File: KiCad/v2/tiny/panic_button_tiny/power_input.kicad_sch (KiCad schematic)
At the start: 3 parts, among them J1 Conn_USB_C_Socket_PowerOnly

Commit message: [UPDATE] the structure of the KiCad design for the tiny version
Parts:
- added U3: ME6211C33M5, Package_TO_SOT_SMD:SOT-23-5, symbol Regulator_Linear:ME6211C33M5
- renumbered J1 to J2
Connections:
- net 5V: now also U3.1 (V_{IN})
- net GND: now also U3.2 (V_{SS})
- new net 3.3V: U3.5 (V_{OUT})
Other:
- added sheet Li-ion charging handling (li-ion_charging_handling.kicad_sch)
- note added: "Voltage stepper for the 3.3v line"

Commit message: [UPDATE] the schematic to contain more connections for the battery section
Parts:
- added C2, C4: 10uF, PCM_SparkFun-Capacitor:C_0603_1608Metric, symbol PCM_SparkFun-Capacitor:10uF_0603_10V_20%
- added C3: 1uF_0603_25V, Capacitor_SMD:C_0201_0603Metric_Pad0.64x0.40mm_HandSolder, symbol PCM_4ms_Capacitor:1uF_0603_25V
- added C5: 100nF_Ceramic, Capacitor_THT:C_Disc_D5.0mm_W2.5mm_P2.50mm, symbol PCM_SL_Capacitors:100nF_Ceramic
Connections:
- net 3.3V: now also C4.1
- net 5V: now also U3.3 (CE), C2.1, C3.2
- net GND: now also C2.2, C3.1, C5.1
- new net: C4.2, C5.2

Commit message: [UPDATE] the schematic wirering
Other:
- sheet Li-ion charging handling ports: added PIN+(5V), PIN-(5V); removed none
- moved on the sheet: C3, C4, C5, U3

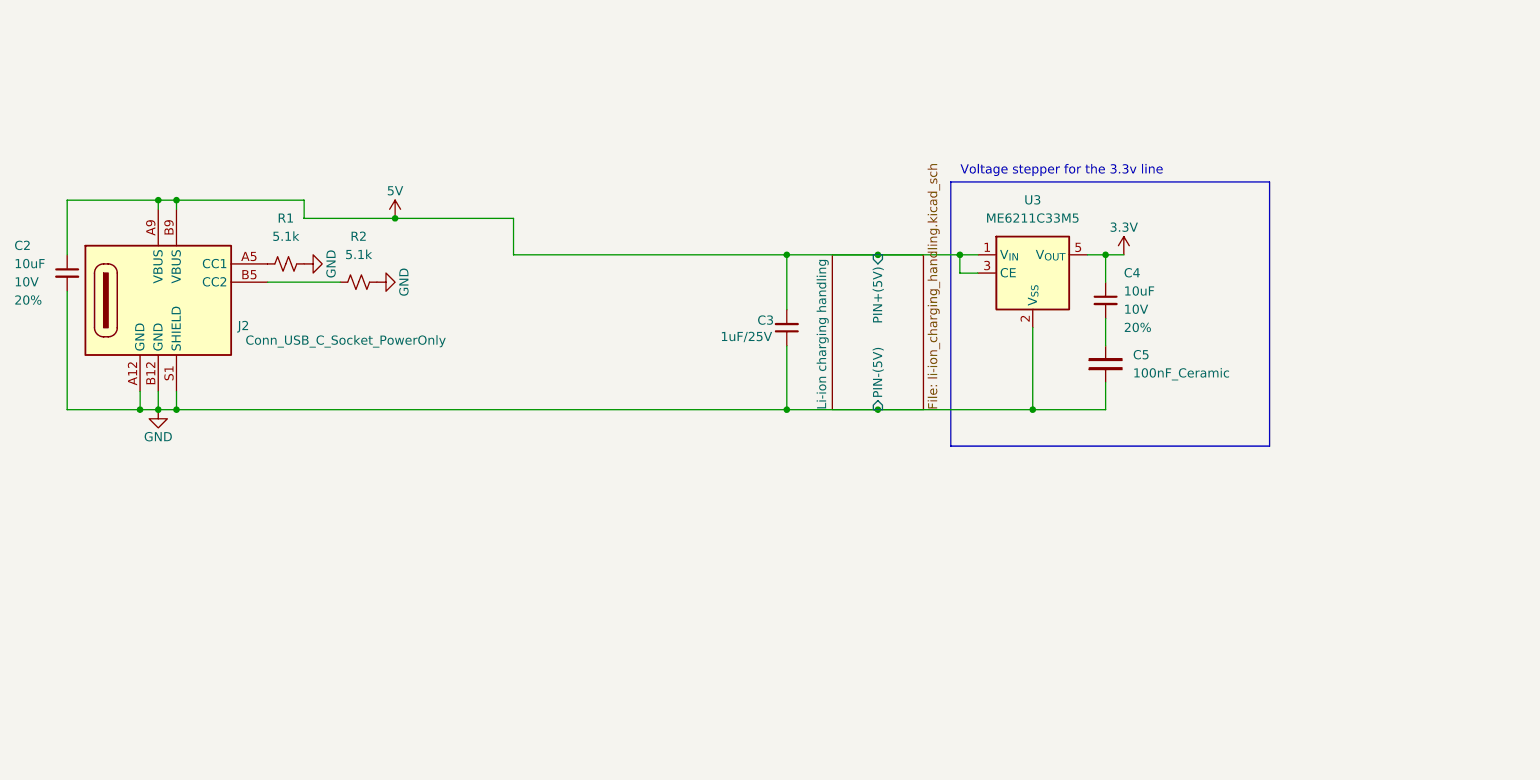
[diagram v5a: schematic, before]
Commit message: [UPDATE] the schematics to hopefully include better connections
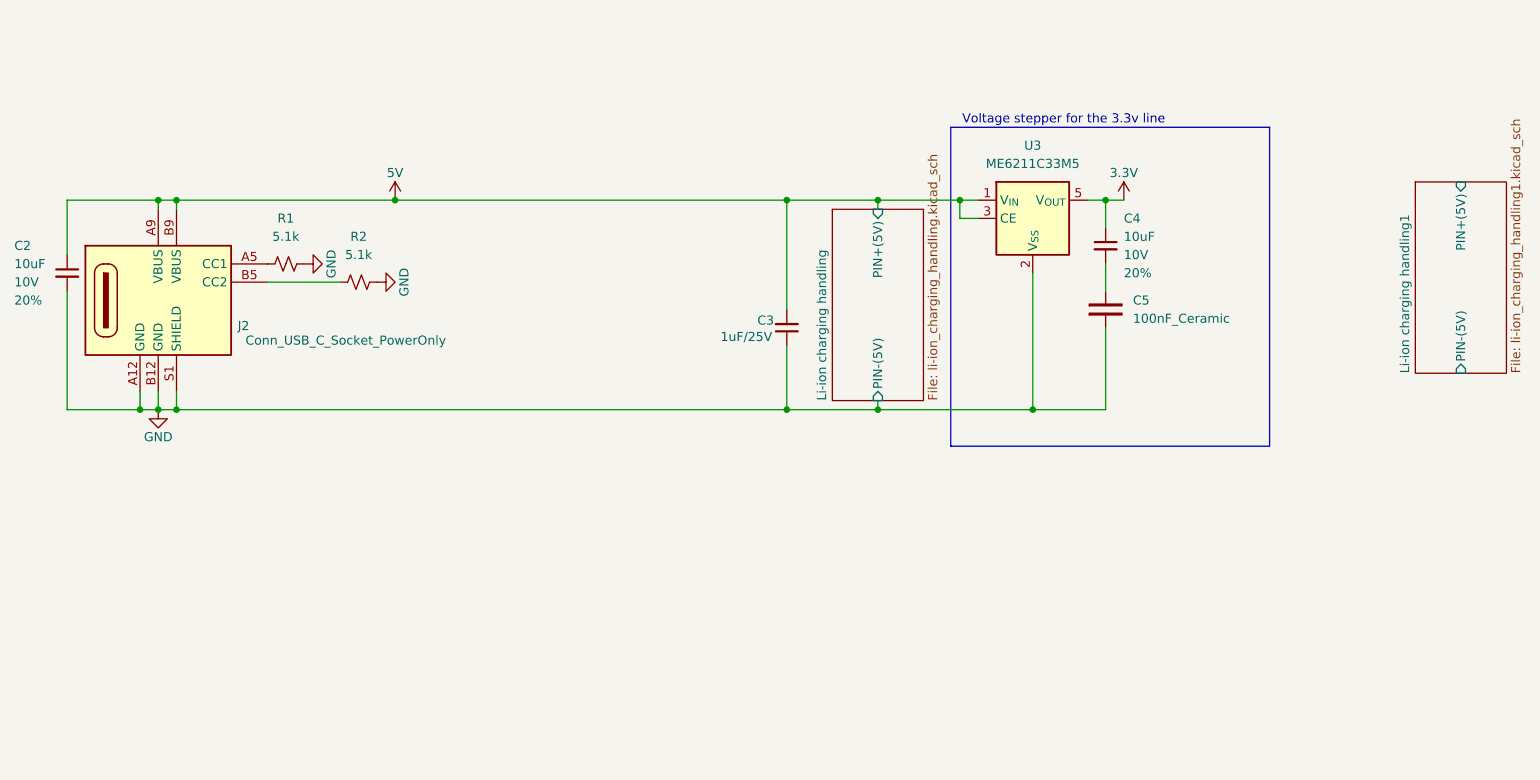
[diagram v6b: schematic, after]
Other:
- added sheet Li-ion charging handling1 (li-ion_charging_handling1.kicad_sch)
- moved on the sheet: C4, C5, U3
